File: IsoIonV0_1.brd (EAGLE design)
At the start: 41.9 x 27.9 mm, 56 parts, among them IC1 MCP3221, IC2 MCP4017-100K, IC4 TL072, IC5 TPS60400DBV

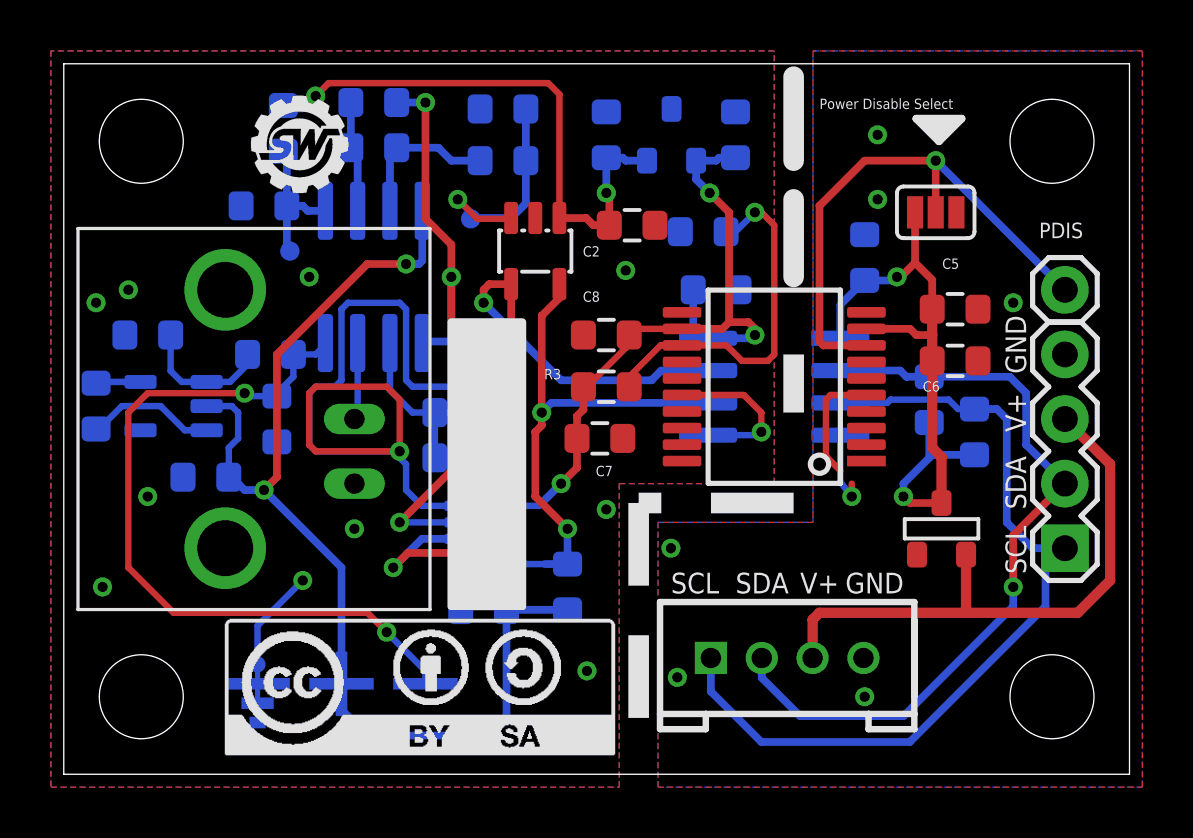
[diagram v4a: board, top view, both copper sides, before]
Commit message: Flip pins on PMos reverse protection FET
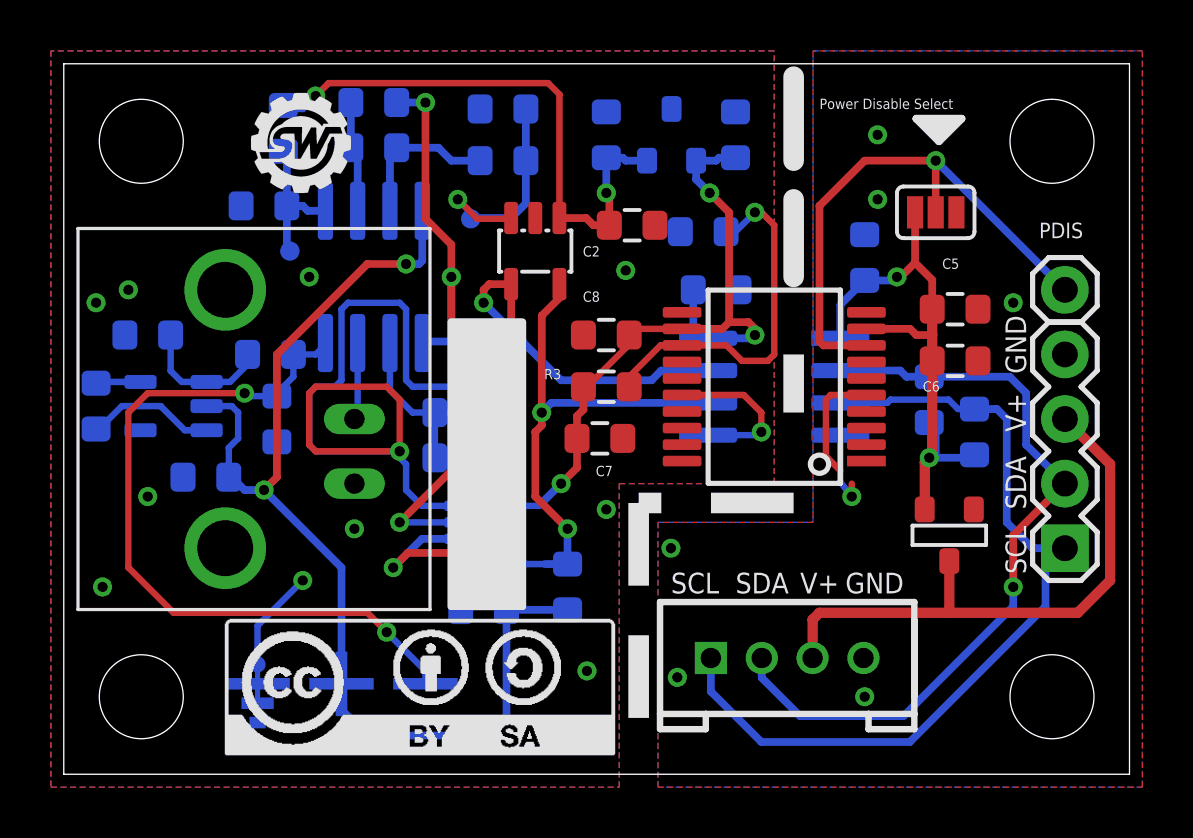
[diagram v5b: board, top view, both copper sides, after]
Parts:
- moved T1 0.36 mm to (34.8, 9.40), turned to 0 degrees
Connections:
- net VCC: now also T1.2; no longer T1.1
- net VIN: now also T1.1; no longer T1.2
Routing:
- net VCC: track 26.3 -> 23.3 mm
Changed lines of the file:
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@@
 <attribute name="VALUE" x="9.779" y="15.24" size="0.4064" layer="28" rot="MR270"/>
 </element>
-<element name="T1" library="SparkysWidgets" package="SOT-23" value="" x="34.544" y="9.652" smashed="yes" rot="R180">
-<attribute name="VALUE" x="35.941" y="7.874" size="1.27" layer="27" ratio="10" rot="R180"/>
+<element name="T1" library="SparkysWidgets" package="SOT-23" value="" x="34.798" y="9.398" smashed="yes">
+<attribute name="VALUE" x="33.401" y="11.176" size="1.27" layer="27" ratio="10"/>
 </element>
 <element name="U$3" library="SW_ArtWork" package="CC-BY-SA" value="CC-BY-SA" x="6.35" y="0.762"/>
@@
 <contactref element="JP5" pad="4"/>
 <contactref element="J1" pad="4"/>
-<contactref element="T1" pad="3"/>
 <polygon width="0.4064" layer="1">
 <vertex x="23.368" y="-0.508"/>
@@
 <via x="24.13" y="3.81" extent="1-16" drill="0.4"/>
 <via x="31.496" y="3.048" extent="1-16" drill="0.4"/>
+<contactref element="T1" pad="3"/>
 </signal>
 <signal name="VCC">
@@
 <contactref element="C14" pad="2"/>
 <contactref element="R15" pad="2"/>
-<contactref element="T1" pad="1"/>
-<wire x1="34.5186" y1="10.668" x2="34.5186" y2="12.4714" width="0.4064" layer="1"/>
-<wire x1="34.5186" y1="12.4714" x2="34.152" y2="12.838" width="0.4064" layer="1"/>
-<wire x1="34.152" y1="16.256" x2="34.152" y2="12.838" width="0.4064" layer="1"/>
+<wire x1="34.152" y1="16.256" x2="34.152" y2="12.33" width="0.4064" layer="1"/>
 <wire x1="34.152" y1="18.288" x2="34.152" y2="17.272" width="0.4064" layer="1"/>
 <wire x1="34.152" y1="17.272" x2="34.152" y2="16.256" width="0.4064" layer="1"/>
@@
 <wire x1="33.285" y1="17.515" x2="33.528" y2="17.272" width="0.3048" layer="1"/>
 <wire x1="34.152" y1="17.272" x2="33.528" y2="17.272" width="0.3048" layer="1"/>
-<wire x1="34.5186" y1="10.668" x2="33.274" y2="10.668" width="0.3048" layer="1"/>
-<wire x1="33.274" y1="10.668" x2="33.02" y2="10.922" width="0.3048" layer="1"/>
-<via x="33.02" y="10.922" extent="1-16" drill="0.4"/>
-<wire x1="33.02" y1="10.922" x2="33.02" y2="11.43" width="0.3048" layer="16"/>
-<wire x1="33.02" y1="11.43" x2="34.036" y2="12.446" width="0.3048" layer="16"/>
-<wire x1="34.036" y1="12.446" x2="34.036" y2="13.832" width="0.3048" layer="16"/>
-<wire x1="35.814" y1="12.562" x2="34.152" y2="12.562" width="0.3048" layer="16"/>
-<wire x1="34.152" y1="12.562" x2="34.036" y2="12.446" width="0.3048" layer="16"/>
 <wire x1="33.4772" y1="22.098" x2="33.4772" y2="20.1168" width="0.3048" layer="1"/>
 <wire x1="33.4772" y1="20.1168" x2="34.152" y2="19.442" width="0.3048" layer="1"/>
@@
 <wire x1="30.54" y1="17.145" x2="30.54" y2="18.464" width="0.3048" layer="16"/>
 <wire x1="30.54" y1="18.464" x2="31.496" y2="19.42" width="0.3048" layer="16"/>
+<contactref element="T1" pad="2"/>
+<wire x1="34.152" y1="12.33" x2="34.036" y2="12.446" width="0.4064" layer="1"/>
+<via x="34.036" y="12.446" extent="1-16" drill="0.4"/>
+<wire x1="34.036" y1="12.446" x2="34.29" y2="12.446" width="0.3048" layer="16"/>
+<wire x1="34.29" y1="12.446" x2="35.698" y2="12.446" width="0.3048" layer="16"/>
+<wire x1="35.698" y1="12.446" x2="35.814" y2="12.562" width="0.3048" layer="16"/>
+<wire x1="34.29" y1="12.446" x2="34.29" y2="13.578" width="0.3048" layer="16"/>
+<wire x1="34.29" y1="13.578" x2="34.036" y2="13.832" width="0.3048" layer="16"/>
+<wire x1="33.8582" y1="10.414" x2="33.8582" y2="12.2682" width="0.4064" layer="1"/>
+<wire x1="33.8582" y1="12.2682" x2="34.036" y2="12.446" width="0.4064" layer="1"/>
 </signal>
 <signal name="VDD">
@@
 <contactref element="JP5" pad="3"/>
 <contactref element="J1" pad="3"/>
-<contactref element="T1" pad="2"/>
 <wire x1="29.448" y1="4.572" x2="29.448" y2="6.08" width="0.4064" layer="1"/>
 <wire x1="29.448" y1="6.08" x2="29.718" y2="6.35" width="0.4064" layer="1"/>
-<wire x1="29.718" y1="6.35" x2="35.56" y2="6.35" width="0.4064" layer="1"/>
-<wire x1="35.56" y1="6.35" x2="39.878" y2="6.35" width="0.4064" layer="1"/>
+<wire x1="29.718" y1="6.35" x2="34.798" y2="6.35" width="0.4064" layer="1"/>
+<wire x1="34.798" y1="6.35" x2="39.878" y2="6.35" width="0.4064" layer="1"/>
 <wire x1="39.878" y1="6.35" x2="41.148" y2="7.62" width="0.4064" layer="1"/>
 <wire x1="41.148" y1="7.62" x2="41.148" y2="12.192" width="0.4064" layer="1"/>
 <wire x1="41.148" y1="12.192" x2="39.37" y2="13.97" width="0.4064" layer="1"/>
-<wire x1="35.4838" y1="8.636" x2="35.4838" y2="6.4262" width="0.4064" layer="1"/>
-<wire x1="35.4838" y1="6.4262" x2="35.56" y2="6.35" width="0.4064" layer="1"/>
+<contactref element="T1" pad="1"/>
+<wire x1="34.8234" y1="8.382" x2="34.8234" y2="6.3754" width="0.4064" layer="1"/>
+<wire x1="34.8234" y1="6.3754" x2="34.798" y2="6.35" width="0.4064" layer="1"/>
 </signal>
 </signals>
-<errors>
-</errors>
 </board>
 </drawing>
